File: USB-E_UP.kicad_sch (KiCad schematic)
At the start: 0 parts

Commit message: labels naming fixes, USB Type E connector added
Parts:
- added D7: ESD122DMXR, EasyEDA:X2SON-3_L1.0-W0.6-L, symbol EasyEDA:ESD122DMXR
- added J13: USB_C_Internal_Connector, symbol Connector:USB_C_Receptacle
- added R68, R69: 5.1k, symbol Device:R
- added U26: TPD4E02B04DQA, Package_SON:USON-10_2.5x1.0mm_P0.5mm, symbol Power_Protection:TPD4E02B04DQA
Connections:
- new net: J13.P8 (CC1), R68.1
- new net: J13.P20 (CC2), R69.1
- new net GND: D7.1 (GND), J13.P14 (GND), J13.P17 (GND), J13.P4 (GND), J13.S1 (SHIELD), R68.2, R69.2, U26.3 (G), U26.8 (G)
- new net USB3_UP.D+: D7.3 (IO2), J13.P19 (D+)
- new net USB3_UP.D-: D7.2 (IO1), J13.18 (D-)
- new net USB3_UP.RX1+: J13.P5 (RX1+), U26.2 (IO2)
- new net USB3_UP.RX1-: J13.P6 (RX1-), U26.1 (IO1)
- new net USB3_UP.TX1+: J13.P2 (TX1+), U26.5 (IO4)
- new net USB3_UP.TX1-: J13.P3 (TX1-), U26.4 (IO3)
- new net VBUS_UP: J13.P1 (VBUS), J13.P11 (VBUS), J13.P7 (VBUS)
- no-connect marks 0 -> 10
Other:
- note added: "USB Connector"

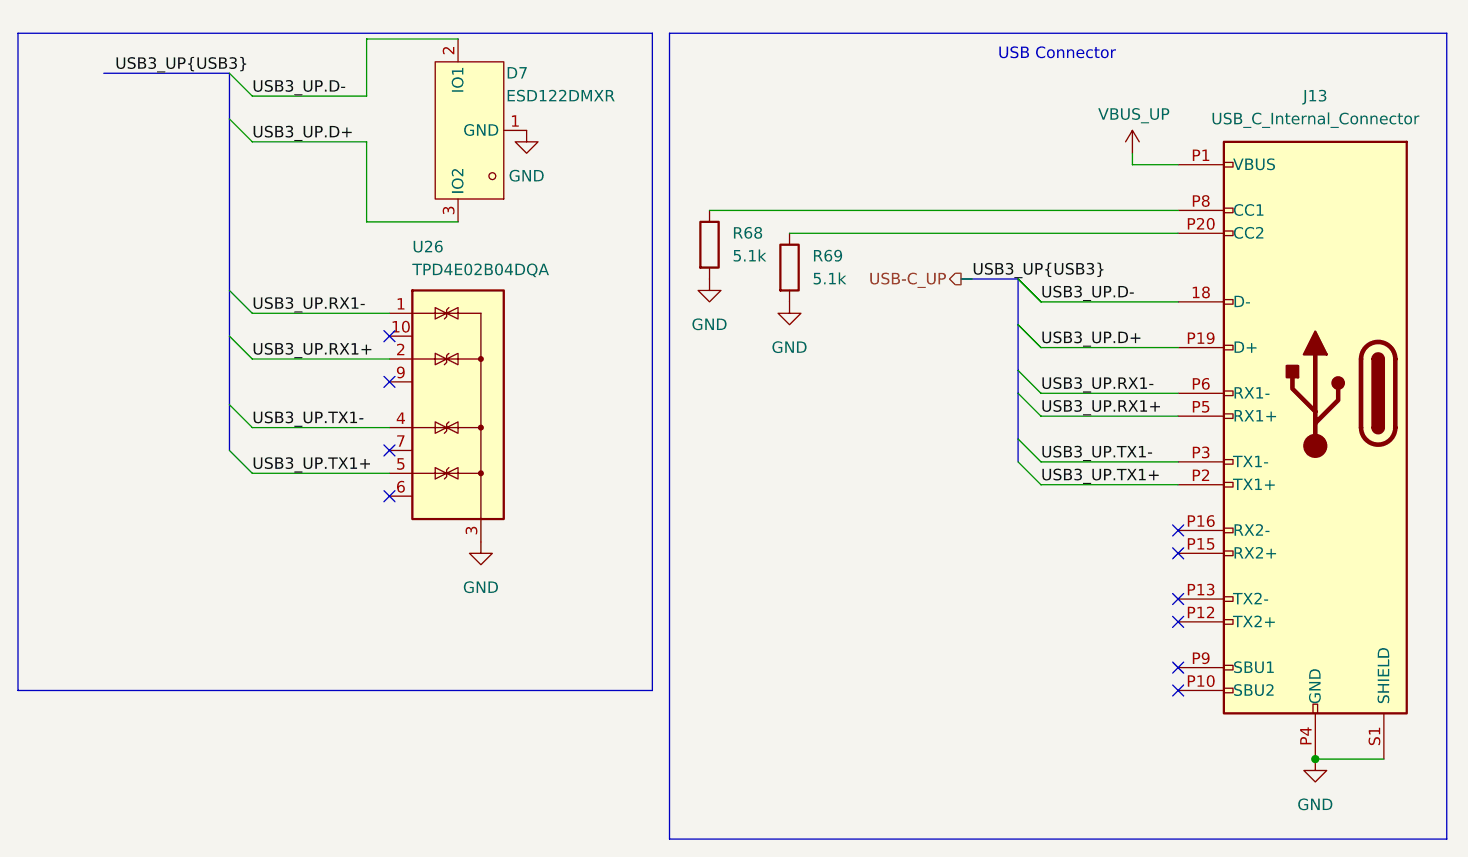
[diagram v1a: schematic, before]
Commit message: TPS25762 EEPROM connector added
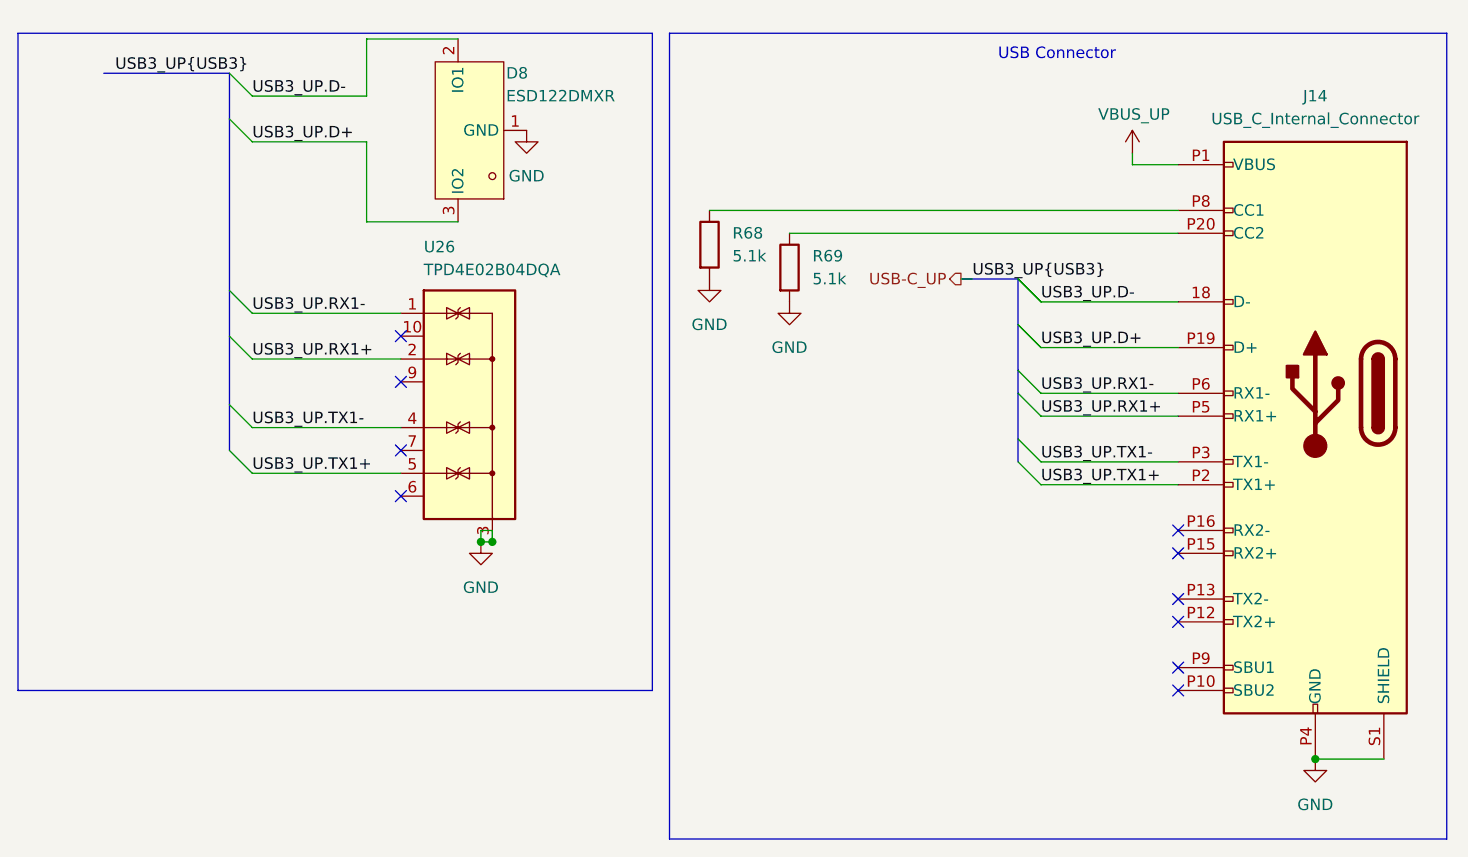
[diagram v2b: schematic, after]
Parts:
- renumbered D7 to D8, J13 to J14
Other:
- title: (none) -> USB Hub
- moved on the sheet: U26
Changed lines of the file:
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@@
 	(generator_version "9.0")
 	(paper "A4")
+	(title_block
+		(title "USB Hub")
+	)
 	(rectangle
 		(start 196.215 13.335)
@@
 		(color 0 0 0 0)
 	)
+	(junction
+		(at 175.26 69.85)
+		(diameter 0)
+		(color 0 0 0 0)
+	)
+	(junction
+		(at 176.53 69.85)
+		(diameter 0)
+		(color 0 0 0 0)
+	)
 	(no_connect
-		(at 165.1 52.07)
+		(at 166.37 52.07)
 	)
 	(no_connect
@@
 	)
 	(no_connect
-		(at 165.1 59.69)
+		(at 166.37 59.69)
 	)
 	(no_connect
@@
 	)
 	(no_connect
-		(at 165.1 64.77)
+		(at 166.37 64.77)
 	)
 	(no_connect
@@
 	)
 	(no_connect
-		(at 165.1 46.99)
+		(at 166.37 46.99)
 	)
 	(no_connect
@@
 	(wire
 		(pts
-			(xy 149.86 57.15) (xy 165.1 57.15)
+			(xy 149.86 57.15) (xy 166.37 57.15)
 		)
 		(stroke
@@
 	(wire
 		(pts
-			(xy 149.86 44.45) (xy 165.1 44.45)
+			(xy 149.86 44.45) (xy 166.37 44.45)
 		)
 		(stroke
@@
 	(wire
 		(pts
-			(xy 149.86 49.53) (xy 165.1 49.53)
+			(xy 176.53 69.85) (xy 175.26 69.85)
+		)
+		(stroke
+			(width 0)
+			(type default)
+		)
+	)
+	(wire
+		(pts
+			(xy 149.86 49.53) (xy 166.37 49.53)
+		)
+		(stroke
+			(width 0)
+			(type default)
+		)
+	)
+	(wire
+		(pts
+			(xy 176.53 69.85) (xy 176.53 68.58)
 		)
 		(stroke
@@
 		)
 	)
+	(wire
+		(pts
+			(xy 175.26 68.58) (xy 175.26 69.85)
+		)
+		(stroke
+			(width 0)
+			(type default)
+		)
+	)
 	(bus
 		(pts
@@
 	(wire
 		(pts
-			(xy 149.86 62.23) (xy 165.1 62.23)
+			(xy 149.86 62.23) (xy 166.37 62.23)
 		)
 		(stroke
@@
 		(pts
 			(xy 234.95 58.42) (xy 234.95 60.96)
+		)
+		(stroke
+			(width 0)
+			(type default)
+		)
+	)
+	(wire
+		(pts
+			(xy 176.53 68.58) (xy 175.26 68.58)
 		)
 		(stroke
@@
 		(dnp no)
 		(fields_autoplaced yes)
-		(property "Reference" "#PWR0206"
+		(property "Reference" "#PWR0209"
 			(at 209.55 49.53 0)
 			(effects
@@
 			(project ""
 				(path "/a2586c28-95f1-49e6-9254-37d7a8473e53/7fe2d266-53fd-4db0-a3a6-d5a75d461820/3d560599-5a8a-4cf0-a02e-a2ff6ae66be7"
-					(reference "#PWR0206")
+					(reference "#PWR0209")
 					(unit 1)
 				)
@@
 		(dnp no)
 		(fields_autoplaced yes)
-		(property "Reference" "#PWR0209"
+		(property "Reference" "#PWR0206"
 			(at 180.34 30.48 0)
 			(effects
@@
 			(project "USB_hub"
 				(path "/a2586c28-95f1-49e6-9254-37d7a8473e53/7fe2d266-53fd-4db0-a3a6-d5a75d461820/3d560599-5a8a-4cf0-a02e-a2ff6ae66be7"
-					(reference "#PWR0209")
+					(reference "#PWR0206")
 					(unit 1)
 				)
@@
 		(dnp no)
 		(fields_autoplaced yes)
-		(property "Reference" "#PWR0208"
+		(property "Reference" "#PWR0210"
 			(at 175.26 76.2 0)
 			(effects
@@
 			(project "USB_hub"
 				(path "/a2586c28-95f1-49e6-9254-37d7a8473e53/7fe2d266-53fd-4db0-a3a6-d5a75d461820/3d560599-5a8a-4cf0-a02e-a2ff6ae66be7"
-					(reference "#PWR0208")
+					(reference "#PWR0210")
 					(unit 1)
 				)
@@
 		(on_board yes)
 		(dnp no)
-		(property "Reference" "J13"
+		(property "Reference" "J14"
 			(at 267.97 20.32 0)
 			(effects
@@
 			(project ""
 				(path "/a2586c28-95f1-49e6-9254-37d7a8473e53/7fe2d266-53fd-4db0-a3a6-d5a75d461820/3d560599-5a8a-4cf0-a02e-a2ff6ae66be7"
-					(reference "J13")
+					(reference "J14")
 					(unit 1)
 				)
@@
 		(on_board yes)
 		(dnp no)
-		(property "Reference" "D7"
+		(property "Reference" "D8"
 			(at 178.054 17.78 0)
 			(effects
@@
 			(project "USB_hub"
 				(path "/a2586c28-95f1-49e6-9254-37d7a8473e53/7fe2d266-53fd-4db0-a3a6-d5a75d461820/3d560599-5a8a-4cf0-a02e-a2ff6ae66be7"
-					(reference "D7")
+					(reference "D8")
 					(unit 1)
 				)
@@
 	(symbol
 		(lib_id "Power_Protection:TPD4E02B04DQA")
-		(at 172.72 54.61 0)
+		(at 173.99 54.61 0)
 		(unit 1)
 		(exclude_from_sim no)
@@
 		(dnp no)
 		(property "Reference" "U26"
-			(at 167.64 37.084 0)
+			(at 168.91 37.084 0)
 			(effects
 				(font
@@
 		)
 		(property "Value" "TPD4E02B04DQA"
-			(at 167.64 39.624 0)
+			(at 168.91 39.624 0)
 			(effects
 				(font
@@
 		)
 		(property "Footprint" "Package_SON:USON-10_2.5x1.0mm_P0.5mm"
-			(at 180.34 54.61 0)
+			(at 181.61 54.61 0)
 			(effects
 				(font
@@
 		)
 		(property "Datasheet" "http://www.ti.com/lit/ds/symlink/tpd4e02b04.pdf"
-			(at 175.26 54.61 0)
+			(at 176.53 54.61 0)
 			(effects
 				(font
@@
 		)
 		(property "Description" "4-Channel ESD Protection Diode for USB Type-C and HDMI 2.0, USON-10"
-			(at 172.72 54.61 0)
+			(at 173.99 54.61 0)
 			(effects
 				(font
@@
 		(dnp no)
 		(fields_autoplaced yes)
-		(property "Reference" "#PWR0207"
+		(property "Reference" "#PWR0208"
 			(at 200.66 46.99 0)
 			(effects
@@
 			(project ""
 				(path "/a2586c28-95f1-49e6-9254-37d7a8473e53/7fe2d266-53fd-4db0-a3a6-d5a75d461820/3d560599-5a8a-4cf0-a02e-a2ff6ae66be7"
-					(reference "#PWR0207")
+					(reference "#PWR0208")
 					(unit 1)
 				)
@@
 		(on_board yes)
 		(dnp no)
-		(property "Reference" "#PWR0205"
+		(property "Reference" "#PWR0207"
 			(at 247.65 30.48 0)
 			(effects
@@
 			(project "USB_hub"
 				(path "/a2586c28-95f1-49e6-9254-37d7a8473e53/7fe2d266-53fd-4db0-a3a6-d5a75d461820/3d560599-5a8a-4cf0-a02e-a2ff6ae66be7"
-					(reference "#PWR0205")
+					(reference "#PWR0207")
 					(unit 1)
 				)

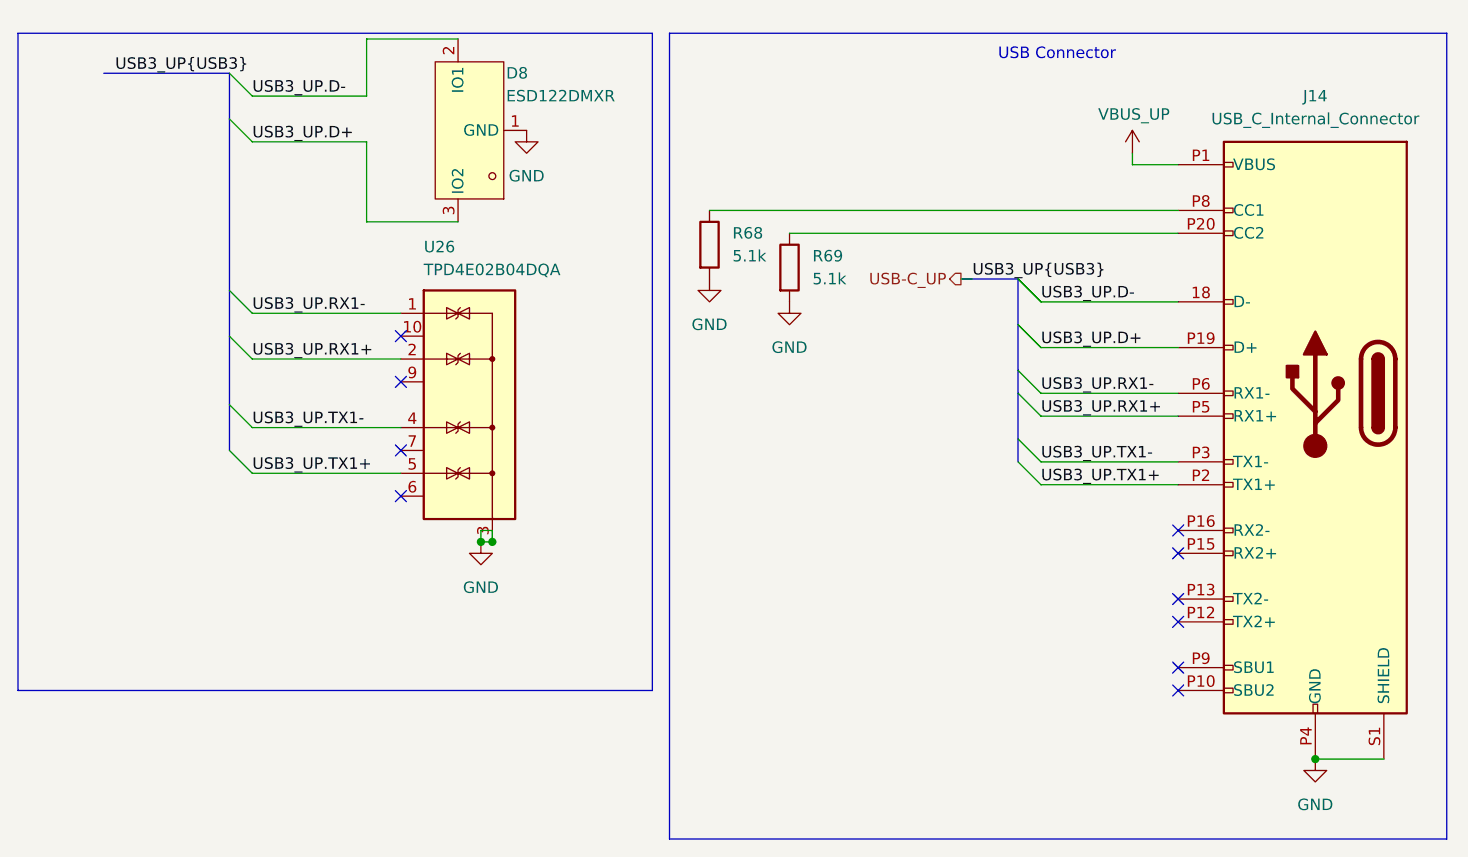
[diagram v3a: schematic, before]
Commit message: Scheme fixes
Fixed wrong connection of SNS pin of U21
USB7206c symbol improved
R7's value fixed
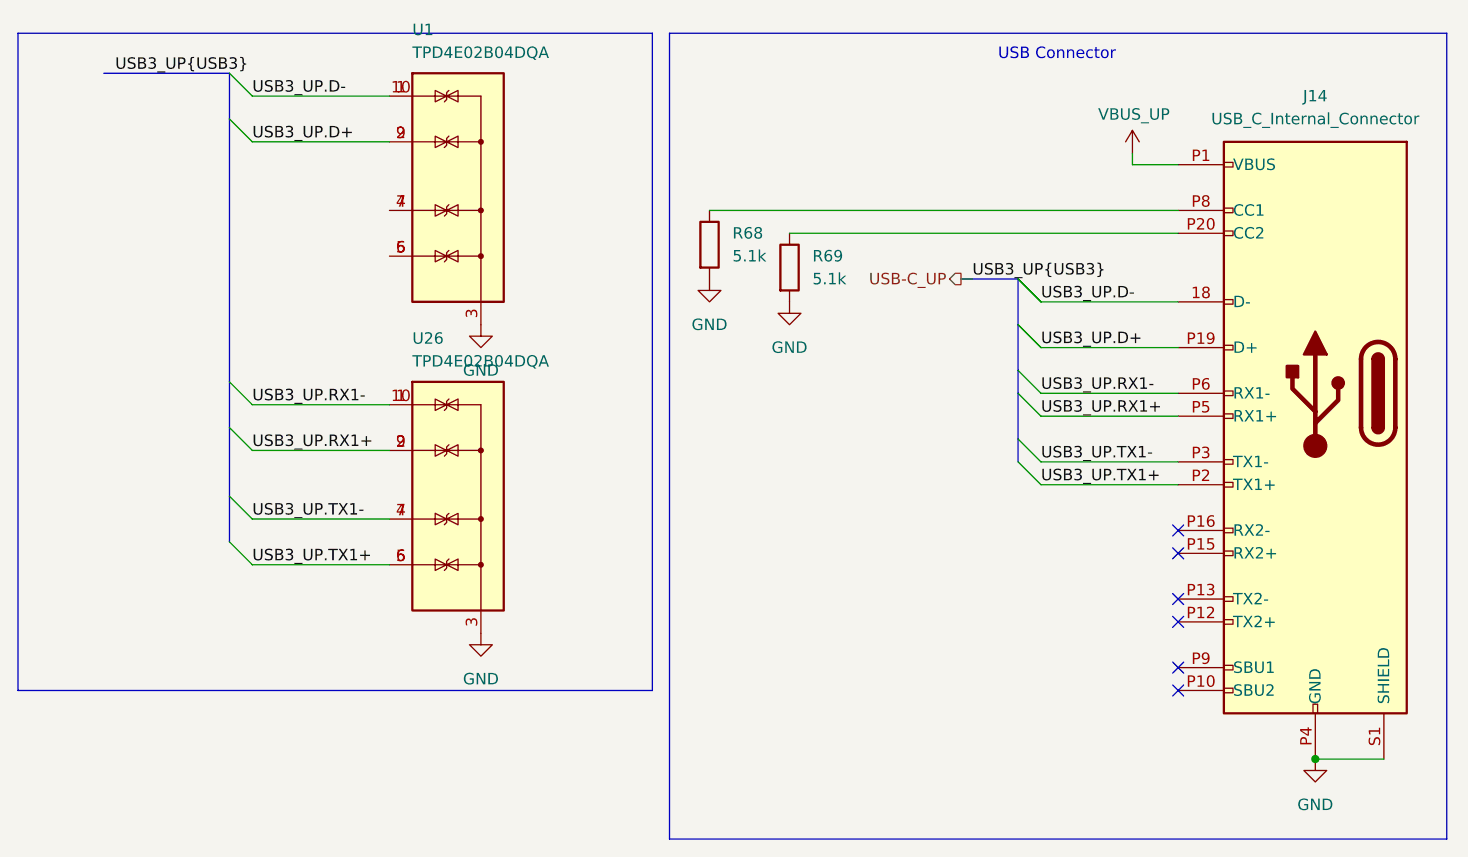
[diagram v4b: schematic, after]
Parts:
- removed D8: ESD122DMXR, EasyEDA:X2SON-3_L1.0-W0.6-L, symbol EasyEDA:ESD122DMXR
- added U1: TPD4E02B04DQA, Package_SON:USON-10_2.5x1.0mm_P0.5mm, symbol Snapeda:TPD4E02B04DQA
- U26: symbol Power_Protection:TPD4E02B04DQA -> Snapeda:TPD4E02B04DQA
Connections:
- net GND: now also U1.3 (G), U1.8 (G)
- net USB3_UP.D+: now also U1.2 (IO2), U1.9 (NC)
- net USB3_UP.D-: now also U1.1 (IO1), U1.10 (NC)
- net USB3_UP.RX1+: now also U26.9 (NC)
- net USB3_UP.RX1-: now also U26.10 (NC)
- net USB3_UP.TX1+: now also U26.6 (NC)
- net USB3_UP.TX1-: now also U26.7 (NC)
- new net: U1.4 (IO3), U1.7 (NC)
- new net: U1.5 (IO4), U1.6 (NC)
- no-connect marks 10 -> 6

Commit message: MCP19035 changed to MP8795
TPS7A4701xRGW to AP7361C-33E
Led Indicator added
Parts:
- renumbered U1 to U25
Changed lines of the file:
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@@
 		)
 		(instances
-			(project ""
-				(path "/a2586c28-95f1-49e6-9254-37d7a8473e53/7fe2d266-53fd-4db0-a3a6-d5a75d461820/3d560599-5a8a-4cf0-a02e-a2ff6ae66be7"
+			(project "USB_hub"
+				(path "/a2586c28-95f1-49e6-9254-37d7a8473e53/df13e2b1-cca0-408c-9316-50e440f0b300"
 					(reference "R68")
 					(unit 1)
@@
 		(dnp no)
 		(fields_autoplaced yes)
-		(property "Reference" "#PWR0209"
+		(property "Reference" "#PWR0197"
 			(at 209.55 49.53 0)
 			(effects
@@
 		)
 		(instances
-			(project ""
-				(path "/a2586c28-95f1-49e6-9254-37d7a8473e53/7fe2d266-53fd-4db0-a3a6-d5a75d461820/3d560599-5a8a-4cf0-a02e-a2ff6ae66be7"
-					(reference "#PWR0209")
+			(project "USB_hub"
+				(path "/a2586c28-95f1-49e6-9254-37d7a8473e53/df13e2b1-cca0-408c-9316-50e440f0b300"
+					(reference "#PWR0197")
 					(unit 1)
 				)
@@
 		(dnp no)
 		(fields_autoplaced yes)
-		(property "Reference" "#PWR0211"
+		(property "Reference" "#PWR0200"
 			(at 267.97 100.33 0)
 			(effects
@@
 		)
 		(instances
-			(project ""
-				(path "/a2586c28-95f1-49e6-9254-37d7a8473e53/7fe2d266-53fd-4db0-a3a6-d5a75d461820/3d560599-5a8a-4cf0-a02e-a2ff6ae66be7"
-					(reference "#PWR0211")
+			(project "USB_hub"
+				(path "/a2586c28-95f1-49e6-9254-37d7a8473e53/df13e2b1-cca0-408c-9316-50e440f0b300"
+					(reference "#PWR0200")
 					(unit 1)
 				)
@@
 		(on_board yes)
 		(dnp no)
-		(property "Reference" "U1"
+		(property "Reference" "U25"
 			(at 167.64 12.954 0)
 			(effects
@@
 		(instances
 			(project "USB_hub"
-				(path "/a2586c28-95f1-49e6-9254-37d7a8473e53/7fe2d266-53fd-4db0-a3a6-d5a75d461820/3d560599-5a8a-4cf0-a02e-a2ff6ae66be7"
-					(reference "U1")
+				(path "/a2586c28-95f1-49e6-9254-37d7a8473e53/df13e2b1-cca0-408c-9316-50e440f0b300"
+					(reference "U25")
 					(unit 1)
 				)
@@
 		(dnp no)
 		(fields_autoplaced yes)
-		(property "Reference" "#PWR0210"
+		(property "Reference" "#PWR0199"
 			(at 175.26 86.36 0)
 			(effects
@@
 		(instances
 			(project "USB_hub"
-				(path "/a2586c28-95f1-49e6-9254-37d7a8473e53/7fe2d266-53fd-4db0-a3a6-d5a75d461820/3d560599-5a8a-4cf0-a02e-a2ff6ae66be7"
-					(reference "#PWR0210")
+				(path "/a2586c28-95f1-49e6-9254-37d7a8473e53/df13e2b1-cca0-408c-9316-50e440f0b300"
+					(reference "#PWR0199")
 					(unit 1)
 				)
@@
 		)
 		(instances
-			(project ""
-				(path "/a2586c28-95f1-49e6-9254-37d7a8473e53/7fe2d266-53fd-4db0-a3a6-d5a75d461820/3d560599-5a8a-4cf0-a02e-a2ff6ae66be7"
+			(project "USB_hub"
+				(path "/a2586c28-95f1-49e6-9254-37d7a8473e53/df13e2b1-cca0-408c-9316-50e440f0b300"
 					(reference "J14")
 					(unit 1)
@@
 		(dnp no)
 		(fields_autoplaced yes)
-		(property "Reference" "#PWR09"
+		(property "Reference" "#PWR0198"
 			(at 175.26 52.07 0)
 			(effects
@@
 		(instances
 			(project "USB_hub"
-				(path "/a2586c28-95f1-49e6-9254-37d7a8473e53/7fe2d266-53fd-4db0-a3a6-d5a75d461820/3d560599-5a8a-4cf0-a02e-a2ff6ae66be7"
-					(reference "#PWR09")
+				(path "/a2586c28-95f1-49e6-9254-37d7a8473e53/df13e2b1-cca0-408c-9316-50e440f0b300"
+					(reference "#PWR0198")
 					(unit 1)
 				)
@@
 		)
 		(instances
-			(project ""
-				(path "/a2586c28-95f1-49e6-9254-37d7a8473e53/7fe2d266-53fd-4db0-a3a6-d5a75d461820/3d560599-5a8a-4cf0-a02e-a2ff6ae66be7"
+			(project "USB_hub"
+				(path "/a2586c28-95f1-49e6-9254-37d7a8473e53/df13e2b1-cca0-408c-9316-50e440f0b300"
 					(reference "R69")
 					(unit 1)
@@
 		(instances
 			(project "USB_hub"
-				(path "/a2586c28-95f1-49e6-9254-37d7a8473e53/7fe2d266-53fd-4db0-a3a6-d5a75d461820/3d560599-5a8a-4cf0-a02e-a2ff6ae66be7"
+				(path "/a2586c28-95f1-49e6-9254-37d7a8473e53/df13e2b1-cca0-408c-9316-50e440f0b300"
 					(reference "U26")
 					(unit 1)
@@
 		(dnp no)
 		(fields_autoplaced yes)
-		(property "Reference" "#PWR0208"
+		(property "Reference" "#PWR0196"
 			(at 200.66 46.99 0)
 			(effects
@@
 		)
 		(instances
-			(project ""
-				(path "/a2586c28-95f1-49e6-9254-37d7a8473e53/7fe2d266-53fd-4db0-a3a6-d5a75d461820/3d560599-5a8a-4cf0-a02e-a2ff6ae66be7"
-					(reference "#PWR0208")
+			(project "USB_hub"
+				(path "/a2586c28-95f1-49e6-9254-37d7a8473e53/df13e2b1-cca0-408c-9316-50e440f0b300"
+					(reference "#PWR0196")
 					(unit 1)
 				)
@@
 		(on_board no)
 		(dnp no)
-		(property "Reference" "#PWR0207"
+		(property "Reference" "#PWR0195"
 			(at 247.65 30.48 0)
 			(effects
@@
 		(instances
 			(project "USB_hub"
-				(path "/a2586c28-95f1-49e6-9254-37d7a8473e53/7fe2d266-53fd-4db0-a3a6-d5a75d461820/3d560599-5a8a-4cf0-a02e-a2ff6ae66be7"
-					(reference "#PWR0207")
-					(unit 1)
-				)
+				(path "/a2586c28-95f1-49e6-9254-37d7a8473e53/df13e2b1-cca0-408c-9316-50e440f0b300"
+					(reference "#PWR0195")
+					(unit 1)
+				)
